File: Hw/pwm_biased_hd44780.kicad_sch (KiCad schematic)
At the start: 21 parts, among them J1 SWD, J2 ETR, SW1 BAT, U1 STM32F030K6Tx, U2 RC1602A, Y2 27MHz

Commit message: use mco
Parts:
- added C3, C4, C5: 100n, symbol Device:C
- D1: value RED -> GREEN
- renumbered C3 to C6, C4 to C7, R3 to R2, R2 to R3
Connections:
- net +3V3: now also C3.2, C4.2
- net GND: now also C3.1, C4.1
- net at U1.18 (PA8): now also U1.22 (PA12), C5.1; no longer U2.11 (DB4)
- new net: C5.2, J2.1 (In)
- new net: U1.13 (PA7), U2.11 (DB4)
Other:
- note added: "MCO"
- note removed: "TIM17_CH1"
- moved on the sheet: BT1, BT2, C6, C7, D1, D3, D4, J1, J2, JP1, R1, R4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

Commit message: upd sch
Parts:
- Y2: value 27MHz -> 25MHz
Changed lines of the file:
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@@
       (effects (font (size 1.27 1.27)) (justify right))
     )
-    (property "Value" "27MHz" (at 86.36 73.66 90)
+    (property "Value" "25MHz" (at 86.36 73.66 90)
       (effects (font (size 1.27 1.27)) (justify right))
     )

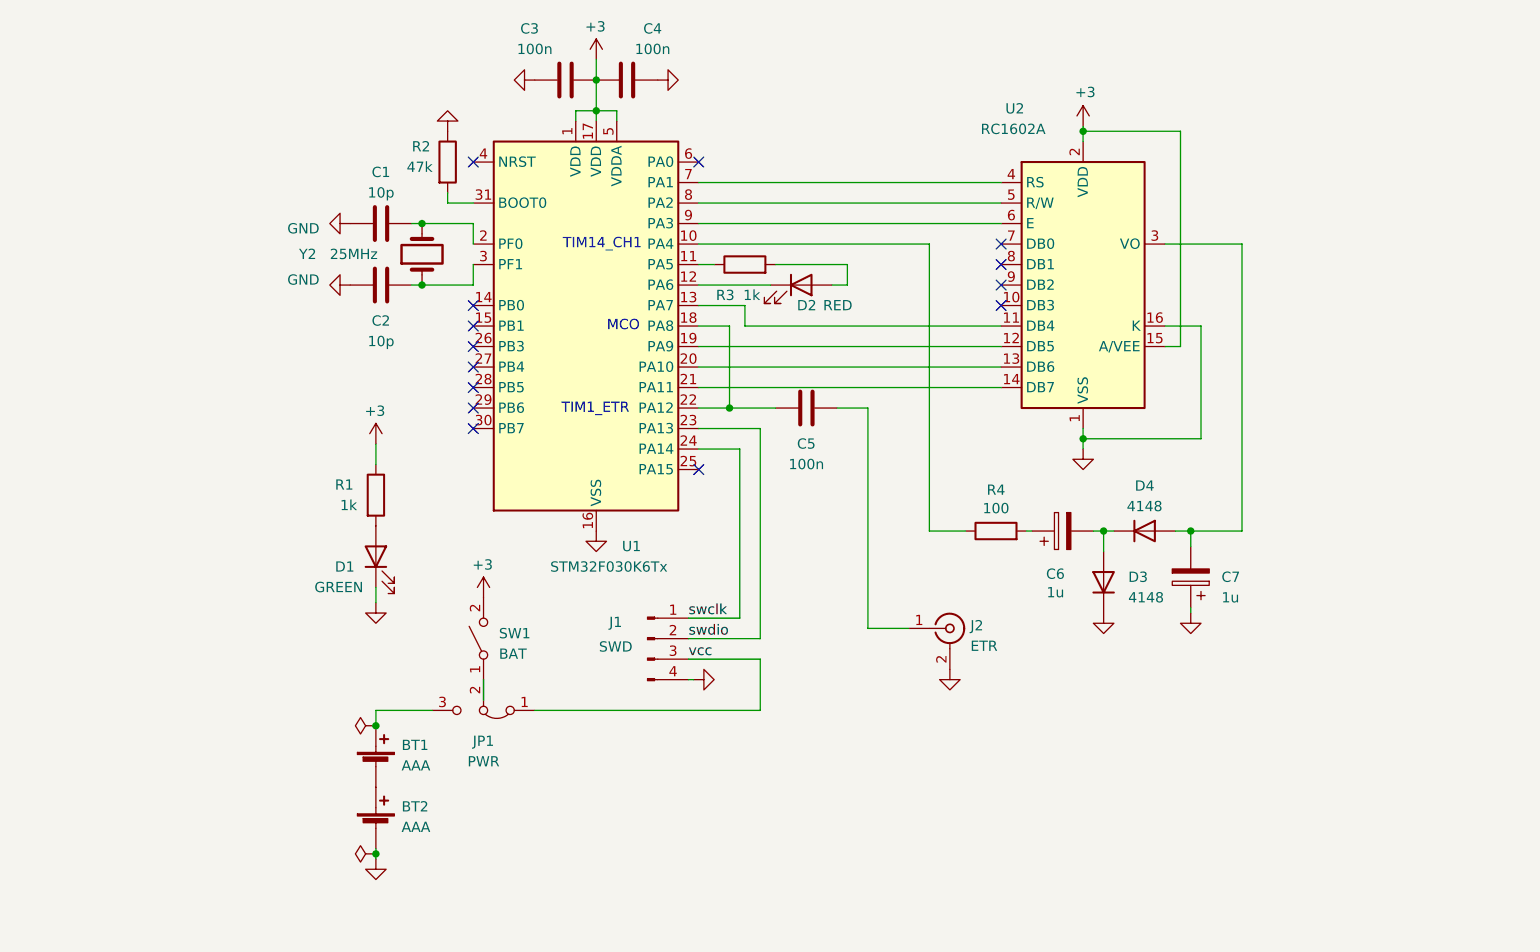
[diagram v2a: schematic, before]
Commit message: timers changed
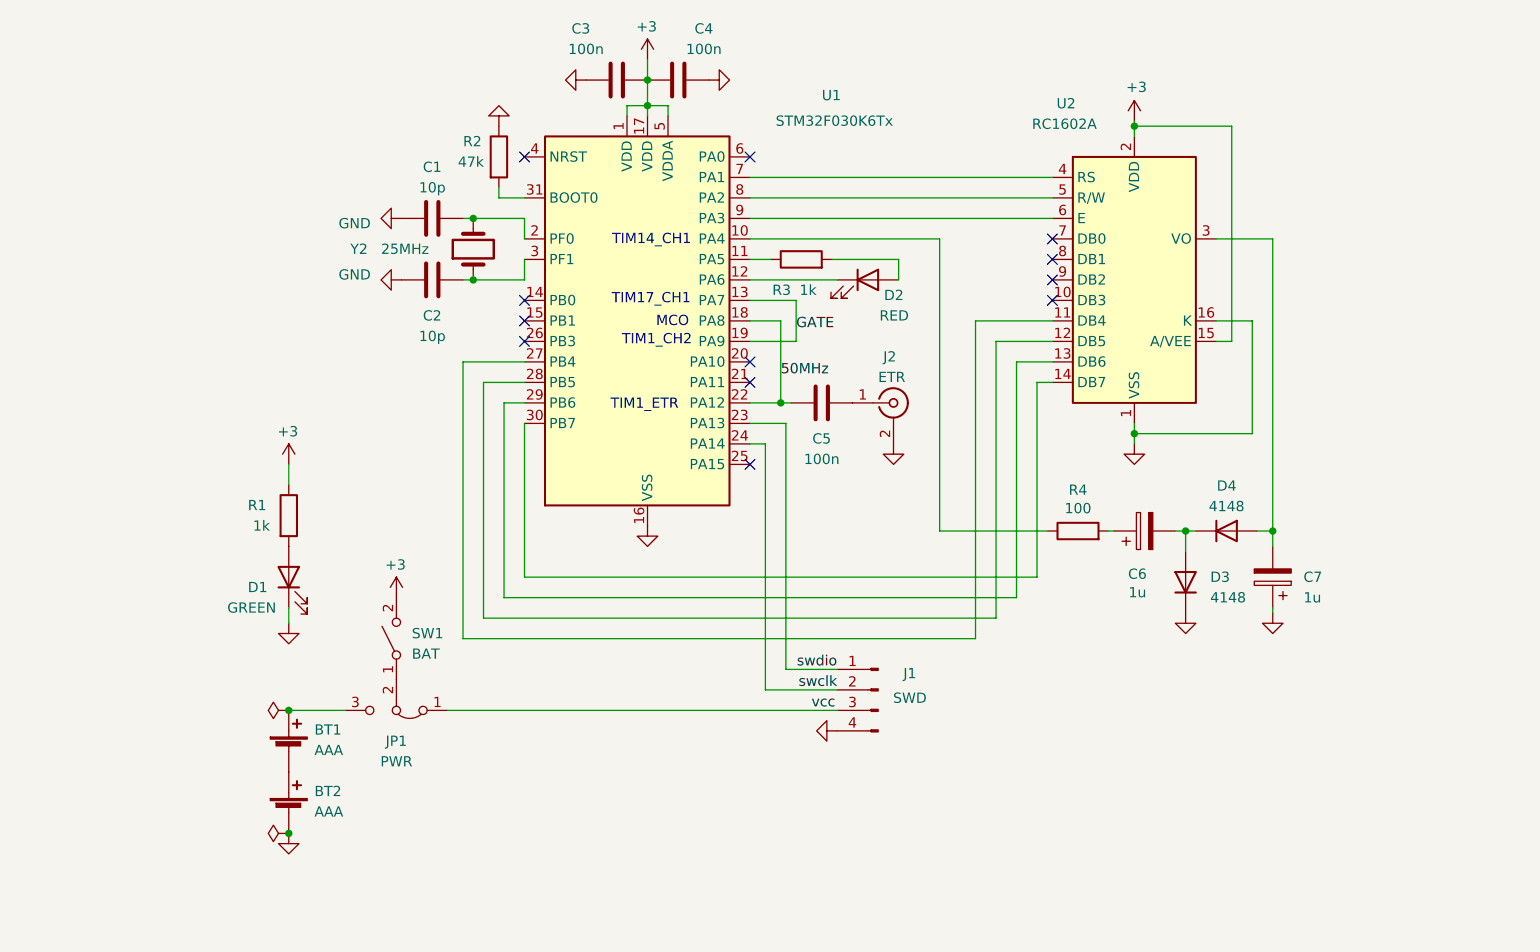
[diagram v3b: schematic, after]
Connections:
- net swclk: now also J1.2 (Pin_2); no longer J1.1 (Pin_1)
- net swdio: now also J1.1 (Pin_1); no longer J1.2 (Pin_2)
- net  50MHz: now reaches C5.1, U1.18 (PA8), U1.22 (PA12)
- net at U2.11 (DB4): now also U1.27 (PB4); no longer U1.13 (PA7)
- net at U2.12 (DB5): now also U1.28 (PB5); no longer U1.19 (PA9)
- net at U1.20 (PA10): no longer U2.13 (DB6)
- net at U1.21 (PA11): no longer U2.14 (DB7)
- net at U1.29 (PB6): now also U2.13 (DB6)
- net at U1.30 (PB7): now also U2.14 (DB7)
- new net  GATE: U1.13 (PA7), U1.19 (PA9)
- no-connect marks 14 -> 12
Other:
- note added: "TIM17_CH1"
- note added: "TIM1_CH2"
- moved on the sheet: BT1, BT2, C1, C2, C3, C4, C5, C6, C7, D1, D2, D3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

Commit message: step back
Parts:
- removed D2: RED, symbol Device:LED
- removed R3: 1k, symbol Device:R
- added C1, C2: 100n, symbol Device:C
- added C3, C4: 8, symbol Device:C
- added D3: RED, symbol Device:LED
- added J1: OUT, symbol Connector:Conn_Coaxial
- added R4: 1k, symbol Device:R
- added U1: Si5351A, Package_SO:MSOP-10_3x3mm_P0.5mm, symbol Oscillator:Si5351A-B-GT
- added Y1: 25 MHz, symbol Device:Crystal
- J3: renamed from J2; value ETR -> IN
- renumbered C6 to C10, C7 to C11, C1 to C5, C2 to C6, C3 to C7, C4 to C8, C5 to C9, D3 to D4, D4 to D5, J1 to J2, R4 to R5, U1 to U2, U2 to U3
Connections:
- net  GATE: no longer U2.13 (PA7), U2.19 (PA9)
- net +3V3: now also C2.1, U1.1 (VDD), U1.7 (VDDO)
- net GND: now also C2.2, C3.2, C4.2, D3.1 (K), J1.2 (Ext), U1.8 (GND)
- net at C9.2, J3.1 (In): now also C1.2, U1.10 (CLK0)
- net at U2.14 (PB0): now also U1.4 (SCL)
- net at U2.15 (PB1): now also U1.5 (SDA)
- net  50MHz: no longer names the net of C9.1, U2.22 (PA12)
- net  50MHz: no longer U2.18 (PA8)
- new net: R4.2, U2.13 (PA7), U2.19 (PA9)
- new net: D3.2 (A), R4.1
- new net: C3.1, U1.2 (XA), Y1.1
- new net: C4.1, U1.3 (XB), Y1.2
- new net: C1.1, J1.1 (In)
- no-connect marks 12 -> 15
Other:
- moved on the sheet: BT1, BT2, C10, C11, C5, C6, C7, C8, C9, D1, D4, D5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
